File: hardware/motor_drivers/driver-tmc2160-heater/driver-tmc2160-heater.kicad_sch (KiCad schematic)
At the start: 80 parts, among them J1 XH, J2 MF3 1x2P, Q1 DMT6016, Q2 DMT6016, Q3 DMT6016, Q4 DMT6016, Q5 DMT6016, Q6 DMT6016, Q7 DMT6016, Q8 DMT6016, Q9 NMOS, T10 CS0, T11 STEP, T12 GND, T13 DIR, T14 EN, T15 HEAT, T16 GND, T17 DIAG, T3 12V, T4 SCK, T5 GND, T6 SDI, T7 SDO, T8 VCC, T9 Therm, U1 TMC2160, U2 UCC27517

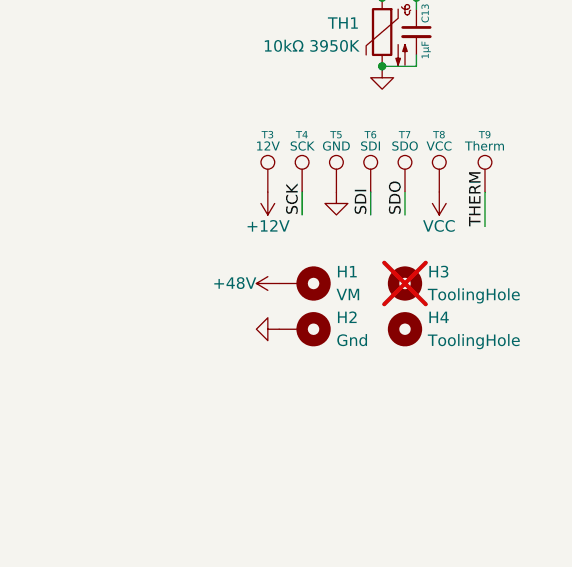
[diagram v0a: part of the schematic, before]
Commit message: Added STEP and Parasolid mechanical files for Corevus-G v0.6, added TMC2160 + Heater module, added toolboard 4x thermistor expansion, added toolboard MAX31856 thermocouple ADC expansion
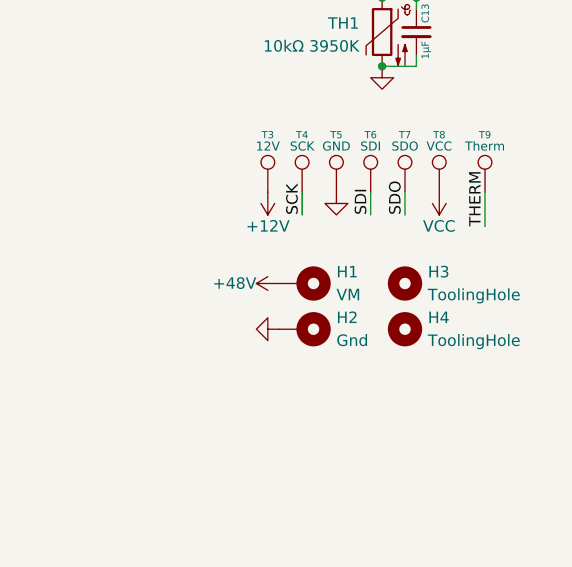
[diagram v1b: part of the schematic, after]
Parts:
- H3: now fitted
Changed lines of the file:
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@@
 		(exclude_from_sim no)
 		(in_bom no)
-		(on_board no)
-		(dnp yes)
+		(on_board yes)
+		(dnp no)
 		(fields_autoplaced yes)
 		(property "Reference" "H3"
